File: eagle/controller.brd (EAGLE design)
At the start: 154.9 x 68.2 mm, 34 parts, among them K1 G5V1, T1 2SC1213, T2 2SC1213, X12 057-040-0

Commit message: First PCB
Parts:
- X1: device con-amp:USB -> con-ptr500:AK500/2
- X11: device con-ptr500:AK500/2 -> con-ptr500:AK500/3-H
- X12: value 057-040-0 -> (none); device con-panduit:057-040-0 -> con-amp:USB
- X13: value (none) -> 057-040-0; device con-phoenix-254:3POL254 -> con-panduit:057-040-0
- moved X13 214.5 mm to (148.6, 72.4), turned to 270 degrees
- moved R1 191.9 mm to (133.3, 49.5), turned to 180 degrees
- moved R2 189.9 mm to (108.0, 87.6)
- moved LED1 189.3 mm to (106.7, 92.7), turned to 180 degrees
- moved X11 184.2 mm to (130.8, 41.9)
- moved X12 172.1 mm to (130.8, 106.7), turned to 180 degrees
- moved X10 158.8 mm to (116.8, 41.9), turned to 180 degrees
- moved X9 135.9 mm to (105.4, 41.9), turned to 180 degrees
- moved X8 113.1 mm to (94.0, 41.9), turned to 180 degrees
- moved R7 103.0 mm to (132.1, 55.9), turned to 0 degrees
- moved X5 93.6 mm to (81.3, 73.7), turned to 90 degrees
- moved X2 91.1 mm to (95.2, 101.6), turned to 0 degrees
- moved SG1 87.7 mm to (123.2, 64.8), turned to 90 degrees
- moved R5 80.2 mm to (111.8, 71.1), turned to 180 degrees
- moved X3 79.9 mm to (81.3, 96.5)
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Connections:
- net GND: now also X1.2, X12.4, X13.6, X2.1; no longer X1.4, X12.6, X13.1, X2.2
- net N$1: now also X1.1, X2.2; no longer X2.1, X5.2
- net N$13: now also X13.13, X8.2; no longer X12.13, X3.2
- net N$15: now also X13.15, X9.2; no longer X12.15, X4.2
- net N$17: now also X13.12; no longer X12.12
- net N$18: now also X10.2, X13.22; no longer X12.22, X6.2
- net N$19: now also X13.7; no longer X12.7
- net N$20: now also X13.1; no longer X12.1
- net N$21: now also X13.16; no longer X12.16
- net N$22: now also R1.2, X12.1, X6.2; no longer X1.1, X11.2
- net N$4: now also X11.2, X3.2, X4.2, X5.2; no longer X10.2, X13.2, X8.2, X9.2
- net N$5: now also X11.3, X13.39; no longer X12.39, X13.3
- net N$6: now also X13.11; no longer X12.11
- net N$9: now also X13.18; no longer X12.18
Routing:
- net GND: track 0.00 -> 302.5 mm
- net N$22: track 0.00 -> 146.0 mm
- net N$4: track 0.00 -> 135.0 mm, vias 0 -> 4
- net N$13: track 0.00 -> 120.8 mm, vias 0 -> 1
- net N$15: track 0.00 -> 97.4 mm, vias 0 -> 1
- net N$18: track 0.00 -> 94.0 mm
- net N$9: track 0.00 -> 77.7 mm, vias 0 -> 1
- net N$21: track 0.00 -> 76.3 mm, vias 0 -> 1
- net N$23: track 0.00 -> 68.7 mm, vias 0 -> 2
- net N$17: track 0.00 -> 65.9 mm, vias 0 -> 1
- net N$20: track 0.00 -> 61.5 mm, vias 0 -> 2
- net N$12: track 0.00 -> 32.5 mm
- net N$8: track 0.00 -> 31.8 mm
- net N$19: track 0.00 -> 29.6 mm
- net N$6: track 0.00 -> 27.1 mm, vias 0 -> 2
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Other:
- board size 154.9 x 68.2 mm -> 81.3 x 74.6 mm

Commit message: Updating PIR
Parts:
- removed R1: 10K, resistor:0204/7
- moved R7 14.2 mm to (119.4, 62.2), turned to 90 degrees
- moved SG1 9.92 mm to (130.8, 58.4)
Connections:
- net N$22: no longer R1.2
- net N$5: now also X13.37; no longer R1.1, X13.39
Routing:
- net N$13: track 120.8 -> 79.6 mm, vias 1 -> 2
- net N$12: track 32.5 -> 63.0 mm, vias 0 -> 1
- net N$18: track 94.0 -> 114.9 mm, vias 0 -> 1
- net N$15: track 97.4 -> 85.6 mm
- net N$23: track 68.7 -> 57.1 mm
- net N$4: track 135.0 -> 145.5 mm
- net N$20: track 61.5 -> 53.4 mm, vias 2 -> 0
- net GND: track 302.5 -> 307.6 mm, vias 0 -> 1
- net N$21: track 76.3 -> 78.5 mm, vias 1 -> 3
- net N$5: track 14.6 -> 12.9 mm
- net N$22: track 146.0 -> 144.3 mm
- net N$8: track 31.8 -> 32.6 mm
- net N$9: vias 1 -> 2
- net N$17: vias 1 -> 2

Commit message: Update
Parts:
- removed T1, T2: 2SC1213, transistor:TO92-EBC
- added T3, T4: 2N2222, transistor-neu-to92:TO92-EBC
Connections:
- net GND: now also T3.E, T4.C; no longer T1.E, T2.E
- net N$10: now also T4.B; no longer T1.B
- net N$12: now also T4.E; no longer T1.C
- net N$2: now also T3.B; no longer T2.B
- net N$3: now also T3.C; no longer T2.C
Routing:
- net N$12: track 63.0 -> 10.5 mm, vias 1 -> 0
- net N$4: track 145.5 -> 99.4 mm, vias 4 -> 2
- net N$23: track 57.1 -> 32.8 mm
- net N$20: track 53.4 -> 33.3 mm
- net GND: track 307.6 -> 327.3 mm
- net N$22: track 144.3 -> 157.5 mm, vias 0 -> 1
- net N$6: track 27.1 -> 20.2 mm, vias 2 -> 0
- net N$3: track 16.3 -> 22.1 mm
- net N$21: track 78.5 -> 83.3 mm, vias 3 -> 2
- net N$18: track 114.9 -> 110.2 mm
- net N$17: track 65.9 -> 70.6 mm, vias 2 -> 0
- net N$2: track 14.6 -> 17.9 mm
- net N$13: track 79.6 -> 76.8 mm, vias 2 -> 3
- net N$19: track 29.6 -> 31.6 mm
- net N$9: track 77.7 -> 79.5 mm, vias 2 -> 1
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
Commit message: First production release
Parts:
- added U$3: (no value), openhardwarelogo:OPEN_HARDWARE_LOGO
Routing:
- net GND: track 327.3 -> 367.5 mm, vias 1 -> 2
- net N$22: track 157.5 -> 192.8 mm
- net N$21: track 83.3 -> 106.0 mm, vias 2 -> 1
- net N$9: track 79.5 -> 71.3 mm, vias 1 -> 2
- net N$15: track 84.7 -> 91.9 mm, vias 2 -> 1
- net N$13: track 76.8 -> 71.4 mm
- net N$23: track 32.8 -> 37.9 mm, vias 2 -> 0
- net N$6: track 20.2 -> 18.1 mm
- net N$17: track 70.6 -> 72.4 mm, vias 0 -> 3
- net N$2: track 17.9 -> 17.1 mm
- net N$4: track 99.4 -> 99.9 mm
- net N$8: track 32.6 -> 32.1 mm, vias 1 -> 0

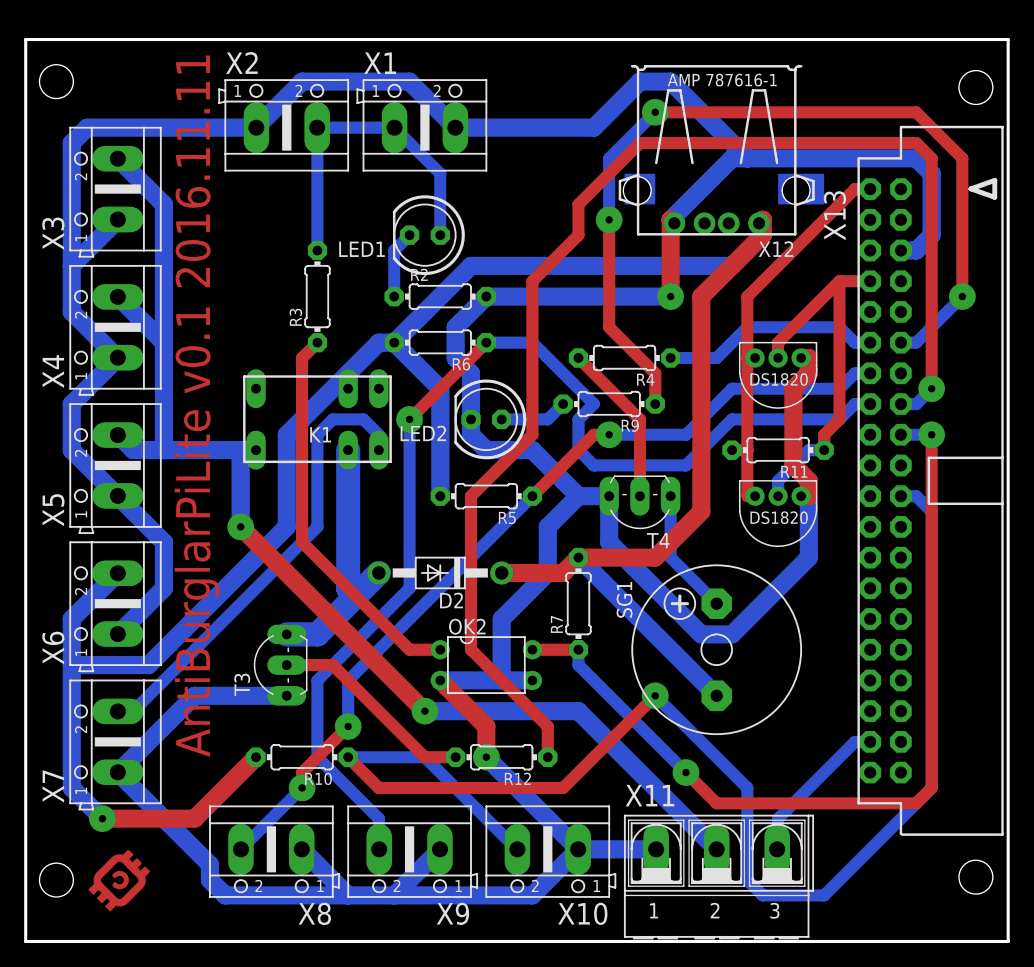
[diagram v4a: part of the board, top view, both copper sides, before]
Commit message: Fixing schematic bug
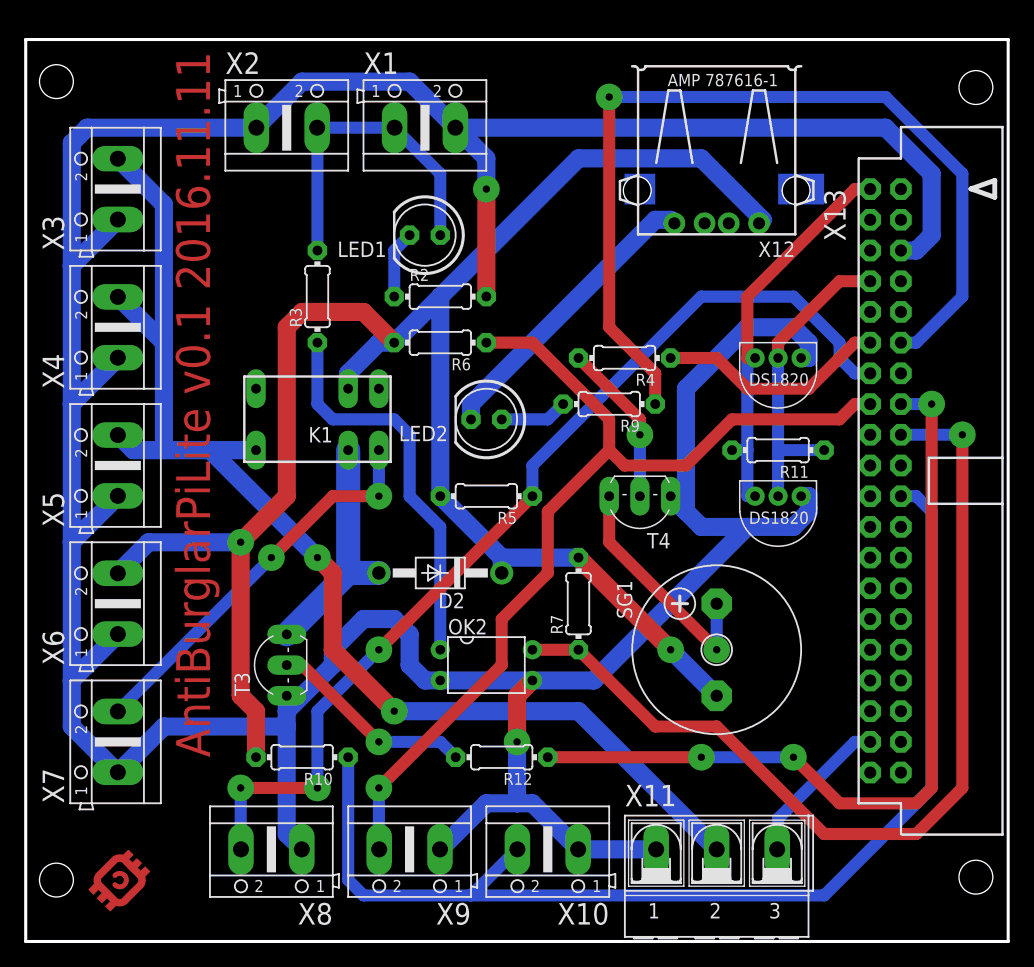
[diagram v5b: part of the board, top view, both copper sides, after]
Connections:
- new net N$11: LED2.K, X12.4
- net GND: now also T4.E; no longer LED2.K, T4.C, X12.4
- net N$12: now also T4.C; no longer T4.E
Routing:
- net GND: track 367.5 -> 326.1 mm
- net N$22: track 192.8 -> 152.3 mm, vias 1 -> 2
- net N$21: track 106.0 -> 68.1 mm, vias 1 -> 3
- net N$11: track 0.00 -> 24.5 mm
- net N$18: track 110.5 -> 94.0 mm, vias 1 -> 0
- net N$15: track 91.9 -> 80.5 mm
- net N$13: track 71.4 -> 82.6 mm
- net N$12: track 10.5 -> 20.2 mm, vias 0 -> 1
- net N$9: track 71.3 -> 77.7 mm, vias 2 -> 1
- net N$19: track 31.6 -> 26.2 mm
- net N$23: track 37.9 -> 32.8 mm, vias 0 -> 2
- net N$17: track 72.4 -> 75.6 mm, vias 3 -> 1
- net N$4: track 99.9 -> 102.4 mm
- net N$3: track 22.1 -> 19.9 mm
- net N$6: track 18.1 -> 19.1 mm
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
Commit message: Small redesign. Bugfixes
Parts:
- removed X2, X3: (no value), con-ptr500:AK500/2
- added D1: 1N5822, diode:DO201T15
- R2, R3: value 1.5K -> 880
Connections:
- removed net N$12: SG1.+, T4.C
- net GND: now also LED2.K, X1.1, X12.4; no longer X1.2, X2.1, X3.1
- net N$1: now also D1.A, X1.2; no longer X1.1, X2.2
- net N$11: now also SG1.-, T4.C; no longer LED2.K, X12.4
- net N$22: now also SG1.+; no longer SG1.-
- net N$4: now also D1.C; no longer X3.2
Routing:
- net GND: track 326.1 -> 0.00 mm, vias 2 -> 0
- net N$22: track 152.3 -> 0.00 mm, vias 2 -> 0
- net N$4: track 102.4 -> 0.00 mm, vias 2 -> 0
- net N$18: track 94.0 -> 0.00 mm
- net N$13: track 82.6 -> 0.00 mm, vias 3 -> 0
- net N$15: track 80.5 -> 0.00 mm, vias 1 -> 0
- net N$9: track 77.7 -> 0.00 mm, vias 1 -> 0
- net N$17: track 75.6 -> 0.00 mm, vias 1 -> 0
- net N$21: track 68.1 -> 0.00 mm, vias 3 -> 0
- net N$20: track 33.5 -> 0.00 mm
- net N$23: track 32.8 -> 0.00 mm, vias 2 -> 0
- net N$8: track 32.6 -> 0.00 mm
- net N$1: track 27.0 -> 0.00 mm
- net N$19: track 26.2 -> 0.00 mm
- net N$11: track 24.5 -> 0.00 mm
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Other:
- board text added: "AntiBurglarPiLite v0.1a 2016.12.01"
- board text removed: "AntiBurglarPiLite v0.1 2016.11.11"

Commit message: Board update
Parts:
- removed X10: (no value), con-ptr500:AK500/2
- removed X11: (no value), con-ptr500:AK500/3-H
- added X2, X3: (no value), con-ptr500:AK500/2
- X9: device con-ptr500:AK500/2 -> con-ptr500:AK500/3-H
- moved D1 65.6 mm to (94.0, 94.0), turned to 90 degrees
- moved X1 25.9 mm to (81.3, 96.5), turned to 90 degrees
- moved X7 25.7 mm to (105.4, 41.9), turned to 180 degrees
- moved X9 25.4 mm to (130.8, 41.9), turned to 0 degrees
- moved X6 24.0 mm to (94.0, 41.9), turned to 180 degrees
- moved X4 22.9 mm to (81.3, 62.2)
- moved X5 22.9 mm to (81.3, 50.8)
- moved X8 22.9 mm to (116.8, 41.9)
- moved LED1 7.73 mm to (105.4, 100.3), turned to 0 degrees
- moved R6 5.68 mm to (113.0, 86.4)
- moved R3 5.68 mm to (100.3, 92.7)
- moved R2 4.58 mm to (110.5, 91.4)
- moved LED2 2.84 mm to (110.5, 80.0)
- moved X12 2.84 mm to (128.3, 108.0)
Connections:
- net GND: now also X2.1, X3.1; no longer X10.1, X11.1
- net N$13: now also X6.2; no longer X8.2
- net N$15: now also X7.2; no longer X9.2
- net N$18: now also X8.2; no longer X10.2
- net N$22: now also X4.2; no longer X6.2
- net N$23: now also X5.2; no longer X7.2
- net N$4: now also X2.2, X3.2, X9.2; no longer X11.2, X4.2, X5.2
- net N$5: now also X9.3; no longer X11.3
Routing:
- net GND: track 0.00 -> 299.5 mm, vias 0 -> 1
- net N$22: track 0.00 -> 156.0 mm, vias 0 -> 1
- net N$21: track 0.00 -> 123.2 mm, vias 0 -> 2
- net N$15: track 0.00 -> 105.8 mm
- net N$4: track 0.00 -> 103.7 mm, vias 0 -> 2
- net N$13: track 0.00 -> 90.6 mm, vias 0 -> 4
- net N$18: track 0.00 -> 88.8 mm, vias 0 -> 1
- net N$9: track 0.00 -> 71.8 mm, vias 0 -> 1
- net N$17: track 0.00 -> 53.4 mm, vias 0 -> 1
- net N$8: track 0.00 -> 38.7 mm
- net N$20: track 0.00 -> 33.3 mm
- net N$23: track 0.00 -> 32.8 mm, vias 0 -> 2
- net N$19: track 0.00 -> 29.6 mm
- net N$1: track 0.00 -> 29.5 mm
- net N$11: track 0.00 -> 25.3 mm
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
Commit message: Board update
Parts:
- moved U$3 11.4 mm to (81.3, 50.8)
- moved X5 9.25 mm to (83.8, 41.9), turned to 180 degrees
- moved X7 1.27 mm to (106.7, 41.9)
- moved X9 1.27 mm to (132.1, 41.9)
- moved X6 1.27 mm to (95.2, 41.9)
- moved X8 1.27 mm to (118.1, 41.9)
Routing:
- net N$13: track 90.6 -> 144.1 mm, vias 4 -> 2
- net GND: track 299.5 -> 344.1 mm, vias 1 -> 4
- net N$21: track 123.2 -> 80.6 mm, vias 2 -> 4
- net N$18: track 88.8 -> 107.5 mm
- net N$15: track 105.8 -> 93.7 mm, vias 0 -> 1
- net N$23: track 32.8 -> 42.0 mm
- net N$9: track 71.8 -> 77.7 mm, vias 1 -> 3
- net N$11: track 25.3 -> 20.2 mm, vias 0 -> 1
- net N$4: track 103.7 -> 108.6 mm, vias 2 -> 3
- net N$22: track 156.0 -> 151.3 mm, vias 1 -> 2
- net N$3: track 19.9 -> 22.1 mm
- net N$8: track 38.7 -> 40.8 mm, vias 0 -> 1
- net N$1: track 29.5 -> 27.6 mm
- net N$19: track 29.6 -> 27.7 mm, vias 0 -> 1
- net N$17: track 53.4 -> 51.9 mm, vias 1 -> 0
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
